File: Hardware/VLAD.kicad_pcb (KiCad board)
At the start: 2 copper layers, 81.8 x 80 mm, 91 parts, among them J1 BMP388, J2 BNO055, J3 Micro_SD_Card, P1 USB_C_Plug_USB2.0, Q1 S8050, Q2 S8050, Q3 S8550, Q4 S8550, Q5 MMBT3904, Q6 MMBT3904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

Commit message: Routed PCB
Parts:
- moved SW1 19.2 mm to (196.8, 64.5)
- moved Q3 5.14 mm to (198.4, 80.8)
- moved R11 5.14 mm to (198.1, 77.7)
- moved R6 5.14 mm to (195.1, 77.7)
- moved R12 5.14 mm to (201.4, 81.3)
- moved SDLED1 5.14 mm to (201.4, 82.8)
- moved C1.1 4.58 mm to (214.6, 99.8), turned to 0 degrees
- moved C5 4.17 mm to (198.1, 84.4)
- moved C6 4.17 mm to (198.1, 86.4)
- moved C2.1 3.06 mm to (214.6, 95.2), turned to 0 degrees
- moved DPower1 2.79 mm to (214.6, 98.3), turned to 0 degrees
- moved TP2 2.29 mm to (195.6, 56.1)
- moved C3.1 2.00 mm to (214.6, 96.8), turned to 0 degrees
- moved TP7 1.55 mm to (192.8, 74.7)
- moved C10 1.52 mm to (212.6, 56.4)
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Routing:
- net +3V3: track 0.00 -> 271.6 mm, vias 0 -> 4
- net /MOSI: track 0.00 -> 102.7 mm, vias 0 -> 3
- net /MISO: track 0.00 -> 86.6 mm, vias 0 -> 2
- net /SCLK: track 0.00 -> 77.8 mm, vias 0 -> 2
- net /USB_RTS: track 0.00 -> 66.8 mm, vias 0 -> 1
- net /RadioCS: track 0.00 -> 56.6 mm, vias 0 -> 1
- net /SerialRx: track 0.00 -> 55.8 mm
- net /SerialTx: track 0.00 -> 53.8 mm
- net /RadioDone: track 0.00 -> 50.9 mm
- net Net-(3V3Regulator1-Pad1): track 0.00 -> 44.7 mm
- net /SDCS: track 0.00 -> 41.7 mm, vias 0 -> 1
- net /USB_DTR: track 0.00 -> 41.2 mm, vias 0 -> 2
- net GND: track 0.00 -> 38.7 mm, vias 0 -> 10
- net /RadioReset: track 0.00 -> 34.4 mm
- net /EN: track 0.00 -> 33.8 mm, vias 0 -> 2
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- added copper zone on B.Cu, net GND
- added copper zone on F.Cu, net GND
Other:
- board size 81.8 x 80 mm -> 81.3 x 76.2 mm

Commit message: Final changes for this first draft
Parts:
- added J4: Conn_01x02_Male, Connector_PinHeader_2.54mm:PinHeader_2x01_P2.54mm_Vertical, F.Cu at (206.2, 98.3)
- added J5: Conn_01x02_Male, Connector_PinHeader_2.54mm:PinHeader_2x01_P2.54mm_Vertical, F.Cu at (175.3, 100.8)
- J1: footprint Connector_PinHeader_2.54mm:PinHeader_1x08_P2.54mm_Vertical -> Connector_PinSocket_2.54mm:PinSocket_1x08_P2.54mm_Vertical
- moved AE1 16.3 mm to (158.0, 106.7)
- moved H1 3.06 mm to (146.6, 110.2)
- moved H3 2.27 mm to (218.2, 42.4)
- moved H4 2.27 mm to (218.2, 110.0)
- moved H2 1.30 mm to (147.1, 42.4)
- moved 3V3Regulator1 1.02 mm to (179.8, 89.7)
- moved C1.2 1.02 mm to (196.8, 97.3)
- moved C1.3 1.02 mm to (196.8, 98.8)
- moved C1.4 1.02 mm to (196.8, 111.3)
- moved C10 1.02 mm to (211.6, 56.4)
- moved C3 1.02 mm to (172.2, 40.1)
- moved C4 1.02 mm to (170.7, 40.1)
- moved C9 1.02 mm to (213.1, 56.4)
- moved D1 1.02 mm to (214.9, 52.6)
- moved D2 1.02 mm to (200.2, 98.0)
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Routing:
- net +6V: track 9.64 -> 21.6 mm
- net +12V: track 8.14 -> 13.2 mm
- net Net-(AE1-Pad1): track 9.47 -> 12.6 mm
- net Net-(3V3Regulator1-Pad1): track 44.7 -> 47.3 mm
- net GND: vias 10 -> 33

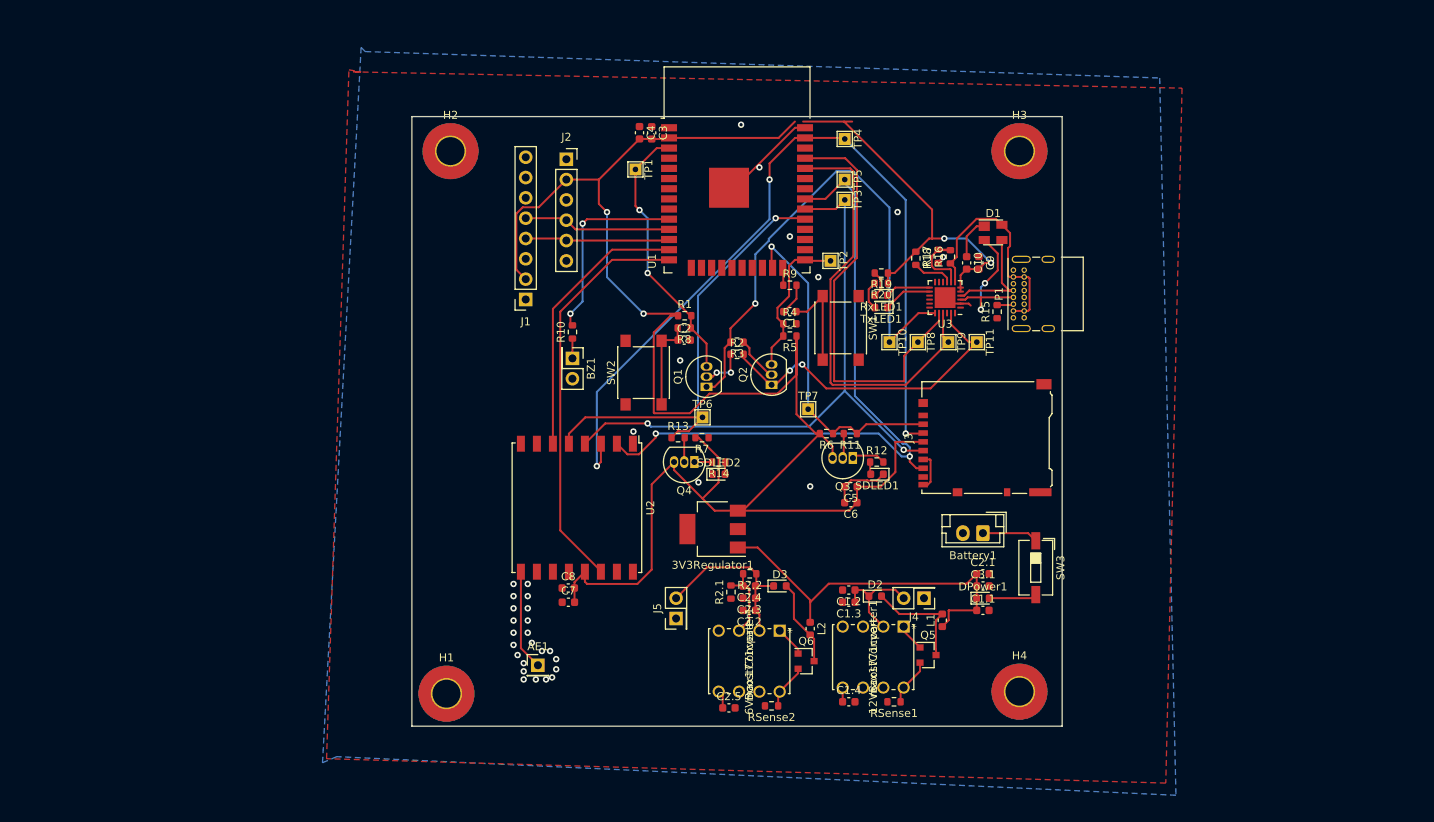
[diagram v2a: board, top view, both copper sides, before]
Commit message: Split PCB setup
Setup the PCB with each section split. J5 didn't have a schematic so I picked one.
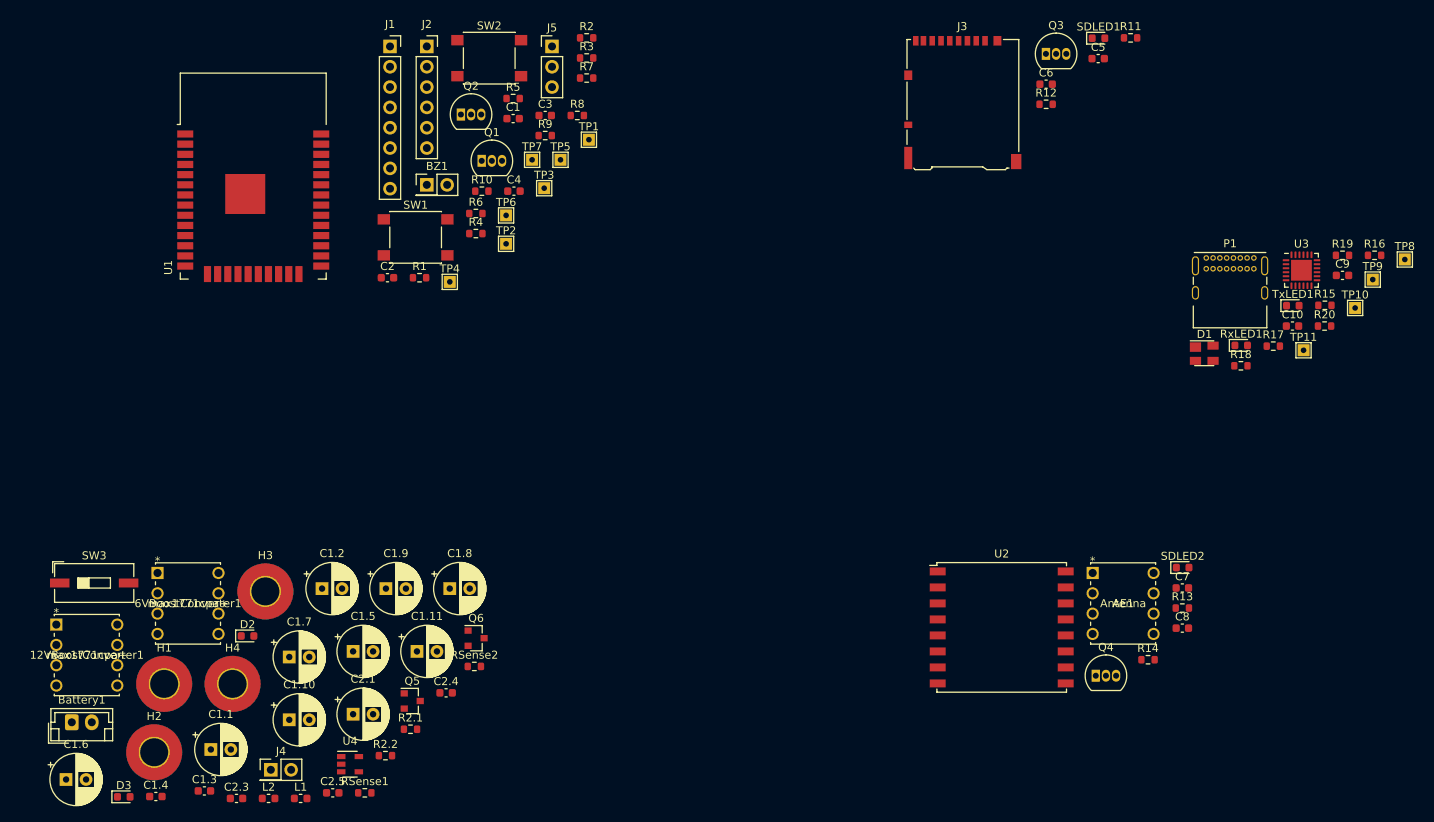
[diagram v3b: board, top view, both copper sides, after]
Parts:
- removed 3V3Regulator1: TC1262-33, Package_TO_SOT_SMD:SOT-223-3_TabPin2
- removed C2.2: 300uF, Capacitor_SMD:C_0603_1608Metric
- removed C3.1: 68uF, Capacitor_SMD:C_0603_1608Metric
- removed DPower1: D, Diode_SMD:D_0603_1608Metric
- added C1.10: 68uF, Capacitor_THT:CP_Radial_D6.3mm_P2.50mm, F.Cu at (126.9, 113.5)
- added C1.11: 68uF, Capacitor_THT:CP_Radial_D6.3mm_P2.50mm, F.Cu at (142.9, 105.0)
- added C1.5: 68uF, Capacitor_THT:CP_Radial_D6.3mm_P2.50mm, F.Cu at (134.9, 105.0)
- added C1.6: 68uF, Capacitor_THT:CP_Radial_D6.3mm_P2.50mm, F.Cu at (99.0, 121.0)
- added C1.7: 68uF, Capacitor_THT:CP_Radial_D6.3mm_P2.50mm, F.Cu at (126.9, 105.7)
- added C1.8: 68uF, Capacitor_THT:CP_Radial_D6.3mm_P2.50mm, F.Cu at (147.0, 97.1)
- added C1.9: 68uF, Capacitor_THT:CP_Radial_D6.3mm_P2.50mm, F.Cu at (139.0, 97.1)
- added U4: MAX40200AUK, Package_TO_SOT_SMD:SOT-23-5, F.Cu at (134.5, 119.1)
- AE1: footprint Connector_PinHeader_2.54mm:PinHeader_1x01_P2.54mm_Vertical -> footprints:max1771cpa&plus_
- C1.1, C2.1: footprint Capacitor_SMD:C_0603_1608Metric -> Capacitor_THT:CP_Radial_D6.3mm_P2.50mm
- C1.2: value 300uF -> 68uF; footprint Capacitor_SMD:C_0603_1608Metric -> Capacitor_THT:CP_Radial_D6.3mm_P2.50mm
- J5: value Conn_01x02_Male -> Conn_01x03_Male; footprint Connector_PinHeader_2.54mm:PinHeader_2x01_P2.54mm_Vertical -> Connector_PinHeader_2.54mm:PinHeader_1x03_P2.54mm_Vertical
- SW3: footprint Button_Switch_SMD:SW_DIP_SPSTx01_Slide_6.7x4.1mm_W6.73mm_P2.54mm_LowProfile_JPin -> Button_Switch_SMD:SW_DIP_SPSTx01_Slide_9.78x4.72mm_W8.61mm_P2.54mm
- moved SW3 117.7 mm to (102.5, 96.4), turned to 0 degrees
- moved Battery1 116.3 mm to (99.7, 113.8), turned to 0 degrees
- moved H3 109.2 mm to (123.9, 97.5)
- moved 12VBoostConverter1 105.9 mm to (97.8, 101.6), turned to 0 degrees
- moved H4 98.4 mm to (119.8, 109.0)
- moved C1.1 98.1 mm to (117.1, 117.2)
- moved C1.4 87.4 mm to (110.2, 123.1)
- moved D3 86.1 mm to (106.2, 123.1)
- moved J4 84.4 mm to (124.6, 119.8), turned to 0 degrees
- moved C1.3 83.9 mm to (116.3, 122.4), turned to 0 degrees
- moved H2 83.8 mm to (110.0, 117.6)
- moved L1 83.2 mm to (128.3, 123.3), turned to 0 degrees
- moved C2.1 80.7 mm to (134.9, 112.8)
- moved D2 78.6 mm to (121.7, 103.0)
- moved 6VBoostConverter1 78.1 mm to (110.4, 95.2), turned to 0 degrees
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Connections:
- C1.1 pad 1: Net-(3V3Regulator1-Pad1) -> +3V3
- C1.2 pad 1: +12V -> +6V
- C2.1 pad 1: Net-(3V3Regulator1-Pad1) -> +3V3
- J5 pad 1: GND -> Net-(J5-Pad1)
- L1 pad 1: Net-(3V3Regulator1-Pad1) -> +3V3
- L2 pad 1: Net-(3V3Regulator1-Pad1) -> +3V3
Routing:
- net +3V3: track 271.6 -> 0.00 mm, vias 4 -> 0
- net /MOSI: track 102.7 -> 0.00 mm, vias 3 -> 0
- net /MISO: track 86.6 -> 0.00 mm, vias 2 -> 0
- net /SCLK: track 77.8 -> 0.00 mm, vias 2 -> 0
- net /USB_RTS: track 66.8 -> 0.00 mm, vias 1 -> 0
- net /RadioCS: track 56.6 -> 0.00 mm, vias 1 -> 0
- net /SerialRx: track 55.8 -> 0.00 mm
- net /SerialTx: track 53.8 -> 0.00 mm
- net /RadioDone: track 50.9 -> 0.00 mm
- net Net-(3V3Regulator1-Pad1): track 47.3 -> 0.00 mm
- net /SDCS: track 41.7 -> 0.00 mm, vias 1 -> 0
- net /USB_DTR: track 41.2 -> 0.00 mm, vias 2 -> 0
- net GND: track 38.7 -> 0.00 mm, vias 33 -> 0
- net /RadioReset: track 34.4 -> 0.00 mm
- net /EN: track 33.8 -> 0.00 mm, vias 2 -> 0
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- removed copper zone on B.Cu, net GND
- removed copper zone on F.Cu, net GND
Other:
- board outline removed

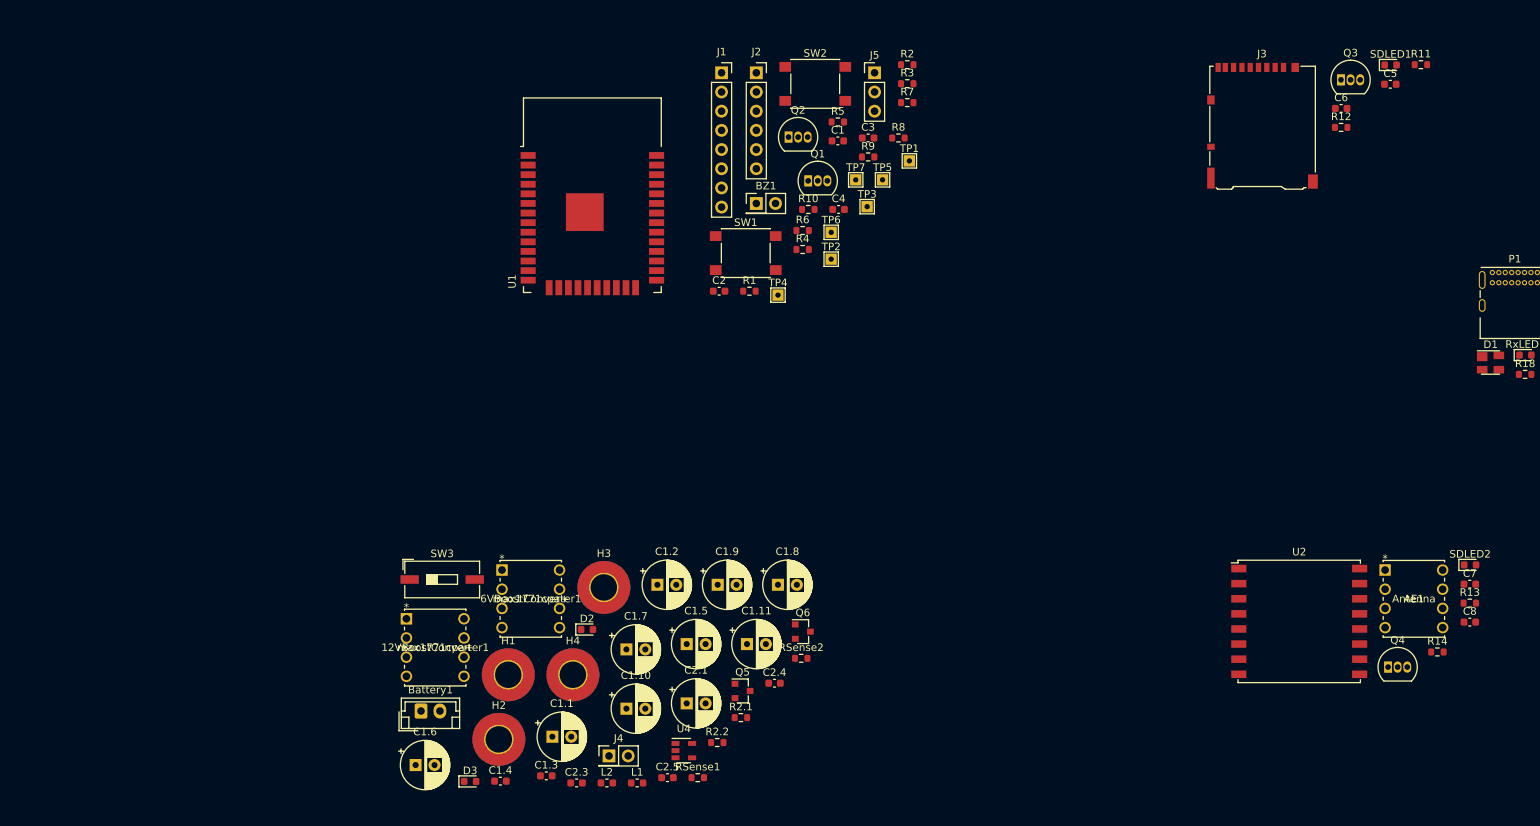
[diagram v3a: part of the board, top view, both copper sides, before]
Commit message: PCB, main ESP32 stuff
My section of the wiring, left some stuff for the top ground fill and for other sections top wires. Could probably tighten the design in some areas.
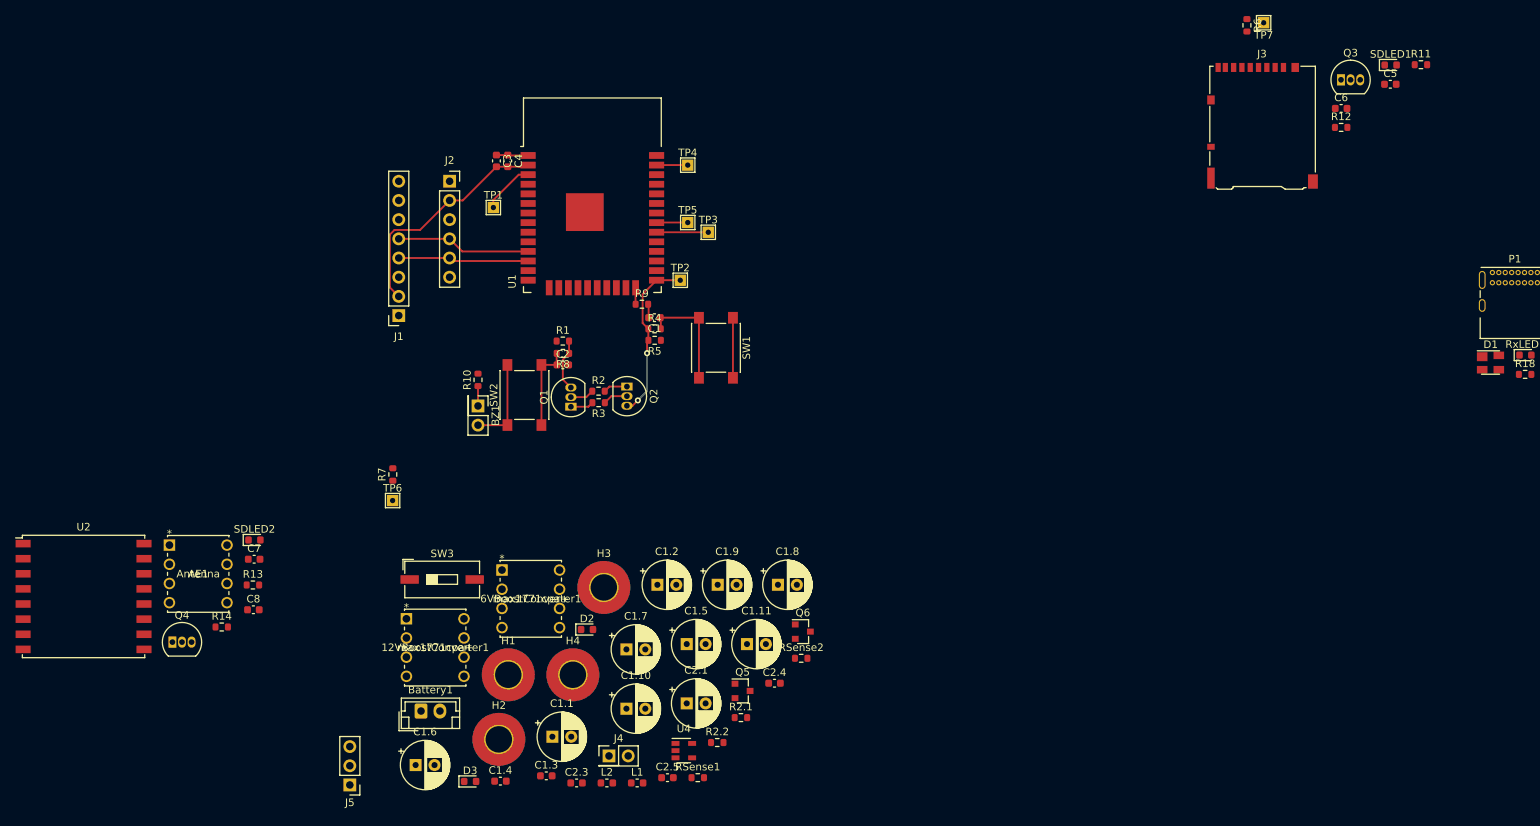
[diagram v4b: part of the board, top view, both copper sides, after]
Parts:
- moved R13 161.1 mm to (77.5, 97.1)
- moved C8 161.0 mm to (77.5, 100.4)
- moved AE1 160.9 mm to (66.4, 91.8)
- moved C7 160.9 mm to (77.6, 93.7)
- moved Q4 160.9 mm to (66.8, 104.7)
- moved R14 160.9 mm to (73.3, 102.7)
- moved SDLED2 160.9 mm to (77.7, 91.2)
- moved U2 160.9 mm to (55.1, 98.6)
- moved J5 117.1 mm to (90.3, 123.6), turned to 180 degrees
- moved R7 84.0 mm to (96.0, 82.5), turned to 90 degrees
- moved TP6 68.0 mm to (96.0, 86.0)
- moved R6 64.8 mm to (209.0, 23.1), turned to 270 degrees
- moved R2 59.5 mm to (123.2, 71.5)
- moved R3 58.8 mm to (123.2, 73.0), turned to 180 degrees
- moved TP7 57.9 mm to (211.3, 22.7), turned to 180 degrees
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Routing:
- net +3V3: track 0.00 -> 30.8 mm
- net GND: track 0.00 -> 25.8 mm
- net /IO0: track 0.00 -> 22.4 mm, vias 0 -> 2
- net /SCL: track 0.00 -> 18.5 mm
- net /SDA: track 0.00 -> 17.8 mm
- net /EN: track 0.00 -> 14.7 mm
- net Net-(C1-Pad1): track 0.00 -> 14.5 mm
- net Net-(C2-Pad1): track 0.00 -> 11.5 mm
- net /SCLK: track 0.00 -> 6.84 mm
- net /MISO: track 0.00 -> 4.13 mm
- net /MOSI: track 0.00 -> 4.13 mm
- net Net-(Q2-Pad2): track 0.00 -> 3.28 mm
- net /USB_DTR: track 0.00 -> 3.19 mm
- net Net-(Q1-Pad2): track 0.00 -> 3.16 mm
- net /USB_RTS: track 0.00 -> 3.07 mm
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
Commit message: Fixed some footprints
Things to bring up:
1. Used a 2N2219 BJT (?) transistor for the sake of circuit connection and footprint. IRL would be using either a 2N2222 (which Palash has in stock) or the one linked on the excel sheet.
2. Used a resistor to break 3.3V bus from the node to prevent wrong connections. IRL will just use a breadboard wire to bridge it, unless more elegant ways of doing this. 
3. Need to sort out the global connection bs idk how to do that.
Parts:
- added Q7: 2N2219, Package_TO_SOT_THT:TO-92_Inline, F.Cu at (148.0, 125.0)
- added R21: R, Resistor_THT:R_Axial_DIN0204_L3.6mm_D1.6mm_P1.90mm_Vertical, F.Cu at (142.0, 132.0)
- D2, D3: footprint Diode_SMD:D_0603_1608Metric -> Diode_THT:D_DO-34_SOD68_P7.62mm_Horizontal
- L1, L2: footprint Inductor_SMD:L_0603_1608Metric -> Inductor_THT:L_Toroid_Vertical_L16.0mm_W8.0mm_P7.62mm
- SW3: footprint Button_Switch_SMD:SW_DIP_SPSTx01_Slide_9.78x4.72mm_W8.61mm_P2.54mm -> Button_Switch_THT:SW_DIP_SPSTx01_Slide_9.78x4.72mm_W7.62mm_P2.54mm
- moved L2 15.1 mm to (110.0, 128.0)
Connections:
- C1.1 pad 1: +3V3 -> Net-(C1.1-Pad1)
- C2.1 pad 1: +3V3 -> Net-(C2.1-Pad1)
- L1 pad 1: +3V3 -> Net-(C1.1-Pad1)
- L2 pad 1: +3V3 -> Net-(C2.1-Pad1)
- U4 pad 5: +3V3 -> Net-(C2.1-Pad1)

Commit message: Power PCB rough layout
Bro im new at this pls save me
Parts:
- moved H3 90.9 mm to (49.0, 149.0)
- moved H1 77.5 mm to (40.3, 140.0)
- moved H4 77.5 mm to (48.8, 140.0)
- moved H2 76.8 mm to (40.0, 149.0)
- moved J5 70.1 mm to (157.0, 145.0), turned to 0 degrees
- moved C2.4 58.8 mm to (88.0, 116.0)
- moved R2.1 58.3 mm to (84.0, 120.0)
- moved Q6 57.2 mm to (95.0, 118.0)
- moved R2.2 55.0 mm to (84.0, 116.0)
- moved SW3 51.7 mm to (99.0, 148.0)
- moved C1.8 51.4 mm to (96.0, 104.0)
- moved J4 48.6 mm to (163.0, 149.5), turned to 90 degrees
- moved Battery1 46.2 mm to (100.0, 160.0), turned to 90 degrees
- moved C2.1 44.8 mm to (94.0, 131.0)
- moved U4 43.9 mm to (108.0, 154.0)
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
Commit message: Added 90mm x 90mm outline and rough layout
I uh don't know how to delete lines lol I hope there's a way otherwise we will have to redo some stuff.
Also I think the capacitors and inductors etc etc are taking up a lot of space. They may need new footprints
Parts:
- moved TP10 214.0 mm to (46.1, 59.0)
- moved C10 214.0 mm to (38.3, 61.3)
- moved D1 214.0 mm to (27.3, 64.7)
- moved P1 214.0 mm to (27.5, 52.8)
- moved R15 214.0 mm to (42.4, 58.7)
- moved R17 214.0 mm to (35.9, 63.8)
- moved R18 214.0 mm to (31.9, 66.3)
- moved RxLED1 214.0 mm to (31.9, 63.7)
- moved TP11 214.0 mm to (39.7, 64.3)
- moved TP8 214.0 mm to (52.4, 53.0)
- moved TP9 214.0 mm to (48.3, 55.5)
- moved TxLED1 214.0 mm to (38.4, 58.7)
- moved U3 214.0 mm to (39.4, 54.3)
- moved C9 214.0 mm to (44.6, 55.0)
- moved R16 214.0 mm to (48.6, 52.4)
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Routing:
- net +6V: track 0.00 -> 54.6 mm
- net +12V: track 0.00 -> 46.1 mm
- net Net-(D2-Pad2): track 0.00 -> 21.4 mm
- net Net-(C1.1-Pad1): track 0.00 -> 21.1 mm
- net Net-(D3-Pad2): track 0.00 -> 20.8 mm
- net Net-(6VBoostConverter1-Pad8): track 0.00 -> 16.4 mm
- net Net-(12VBoostConverter1-Pad8): track 0.00 -> 16.4 mm
- net Net-(C2.1-Pad1): track 0.00 -> 11.4 mm
- net Net-(6VBoostConverter1-Pad3): track 0.00 -> 7.48 mm
- net Net-(6VBoostConverter1-Pad1): track 0.00 -> 5.81 mm
- net Net-(12VBoostConverter1-Pad1): track 0.00 -> 5.81 mm
- net Net-(6VBoostConverter1-Pad5): track 0.00 -> 4.44 mm
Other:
- board outline added: 90 x 90 mm
